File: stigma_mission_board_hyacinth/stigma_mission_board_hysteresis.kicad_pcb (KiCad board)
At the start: 4 copper layers, 50 x 150 mm, 209 parts, among them J1 DF40C-70DS-0.4V(51), J2 DF40HB(2.5)-10DS-0.4V(51), J7 SMA, J8 SMA, J9 JST-GH 4Pin, Q1 DMN2056U, Q2 DMN2056U, Q3 AOSP21321, Q4 DMN2056U, Q5 AOSP21321, Q6 DMN2056U, Q7 AOSP21321, Q8 DMN2056U, Q9 AOSP21321, U1 LAN8742A, U10 MCP2562-E-SN, U11 MCP2562-E-SN, U12 SN74HCS594, U13 INA181, U14 INA181, U15 INA181, U16 INA181, U2 INA181, U3 TPD4E1U06, U4 L7805, U5 L7805, U6 AZ1117H-ADJ, U7 AZ1117H-ADJ, U8 Ai-Thinker-Ra-01, U9 Ai-Thinker-Ra-01, Y1 25MHz

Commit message: Added more components to NEW pcb layout.
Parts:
- removed C37, C54: 1u, Capacitor_SMD:C_0603_1608Metric
- removed C38: 10u, Capacitor_SMD:C_0805_2012Metric
- removed C39, C41: 22u, Capacitor_SMD:C_0805_2012Metric
- removed C46, C48: 10u, Capacitor_SMD:C_1206_3216Metric
- removed C47, C49: 100n, Capacitor_SMD:C_0603_1608Metric
- removed C53: 4u7, Capacitor_SMD:C_0805_2012Metric
- removed D13: SS34, Diode_SMD:D_SMA
- removed D20, D23: NRVB130T1G, Diode_SMD:D_SOD-123
- removed D21, D24: LED, LED_SMD:LED_0603_1608Metric
- removed D22, D25: D, Diode_SMD:D_0603_1608Metric
- removed F5, F6, F7, F8: 10A, Fuse:Fuse_1206_3216Metric
- removed J11, J12, J3: ~, Connector_Molex:Molex_Micro-Fit_3.0_43045-0400_2x02_P3.00mm_Horizontal
- removed JP1: SolderJumper_2_Open, Jumper:SolderJumper-2_P1.3mm_Open_Pad1.0x1.5mm
- removed JP4, JP5: servo_switch, Stigma:SolderJumper-3_Open_RoundedPad2x2mm
- removed Q4, Q6: DMN2056U, Package_TO_SOT_SMD:SOT-23
- removed Q5, Q7: AOSP21321, Package_SO:SO-8_3.9x4.9mm_P1.27mm
- removed R49, R53: 10k, Resistor_SMD:R_0603_1608Metric
- removed R50, R52, R54, R56: 1k, Resistor_SMD:R_0603_1608Metric
- removed R51, R55: 60R, Resistor_SMD:R_0603_1608Metric
- removed Shunt2, Shunt3: 250mR 1%, Resistor_SMD:R_0805_2012Metric
- removed U14, U15: INA181, Package_TO_SOT_SMD:SOT-23-6
- C14, C15, C16, C17, C18, C19, C20, C21, D10, D11, D12, D5, D6, D7, D8, D9, R30, R31, R32, R33, R34, R35, R36, R37, U4, U5, U6, U7: moved to B.Cu
- J1, J2: moved to F.Cu
- moved R23 278.4 mm to (141.3, 192.2)
- moved R25 278.4 mm to (107.2, 192.7)
- moved R26 278.4 mm to (107.2, 189.6)
- moved R24 278.4 mm to (141.3, 189.2)
- moved C51 273.9 mm to (125.8, 243.7)
- moved C55 273.9 mm to (123.2, 242.4)
- moved D26 273.9 mm to (124.8, 236.5)
- moved D27 273.9 mm to (113.4, 228.6)
- moved F1 273.9 mm to (121.6, 243.4)
- moved JP6 273.9 mm to (120.8, 238.5)
- moved Q8 273.9 mm to (127.3, 231.1)
- moved Q9 273.9 mm to (120.4, 232.3)
- moved R58 273.9 mm to (124.9, 231.1)
- moved R60 273.9 mm to (116.8, 228.6)
- moved Shunt4 273.9 mm to (126.0, 238.6)
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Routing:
- net GND: track 58.5 -> 26.5 mm, vias 43 -> 22
- net Net-(U15-+): track 7.55 -> 0.00 mm
- net Net-(U14-+): track 6.38 -> 0.00 mm
- net Net-(D20-A): track 4.93 -> 0.00 mm
- net Net-(D23-A): track 4.75 -> 0.00 mm
- net /Recovery Output 4/recovery_switched: track 4.73 -> 0.00 mm
- net /Recovery Output2/recovery_switched: track 3.54 -> 0.00 mm
- net +3.3V: track 3.16 -> 0.00 mm
- net /Recovery Output2/high_current: track 2.54 -> 0.00 mm, vias 16 -> 0
- net /Recovery Output 4/high_current: track 2.54 -> 0.00 mm, vias 15 -> 0
- net /Recovery Output 4/servo_line: track 2.36 -> 0.00 mm
- net /Recovery Output2/servo_line: track 2.26 -> 0.00 mm
- net RECOVERY_4: track 1.86 -> 0.00 mm
- net RECOVERY_2: track 1.80 -> 0.00 mm
- net Net-(D24-A): track 1.39 -> 0.00 mm
- removed copper zone on B.Cu, net /Recovery Output 1/high_current
- removed copper zone on B.Cu, net /Recovery Output 4/high_current
- removed copper zone on F.Cu, net /Recovery Output 4/high_current
- removed copper zone on F.Cu, net /Recovery Output 4/recovery_switched
- removed copper zone on F.Cu, net /Recovery Output 4/servo_line
- removed copper zone on B.Cu, net /Recovery Output2/high_current
- removed copper zone on F.Cu, net /Recovery Output2/high_current
- removed copper zone on F.Cu, net /Recovery Output2/recovery_switched
- removed copper zone on F.Cu, net /Recovery Output2/servo_line
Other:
- board size 50 x 150 mm -> 16.4 x 9.5 mm
- board text removed: "LORA"
- board text removed: "recovery1"
- board text removed: "recovery2"
- board text removed: "recovery3"
- board text removed: "recovery4"
- board text removed: "take a look"
- board text removed: "todo: symmetrize"

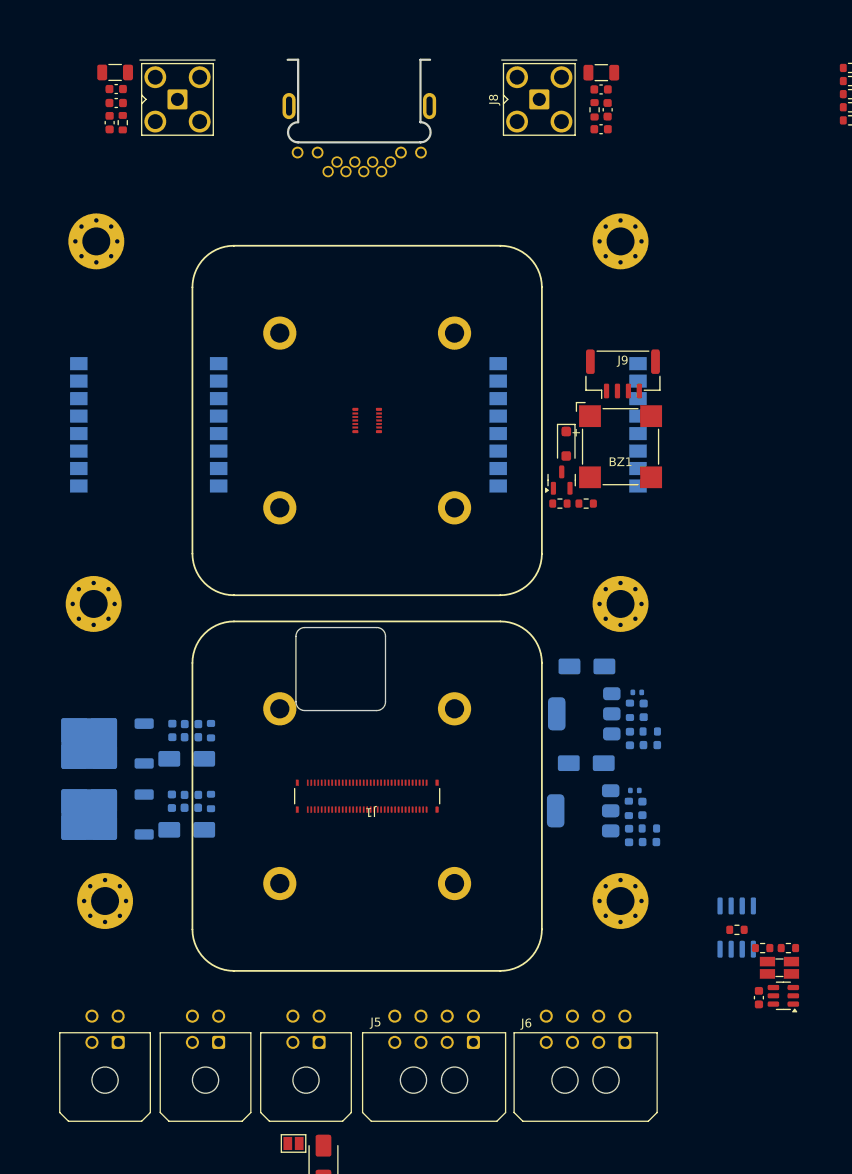
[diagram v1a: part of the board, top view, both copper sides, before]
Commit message: changed outer layout
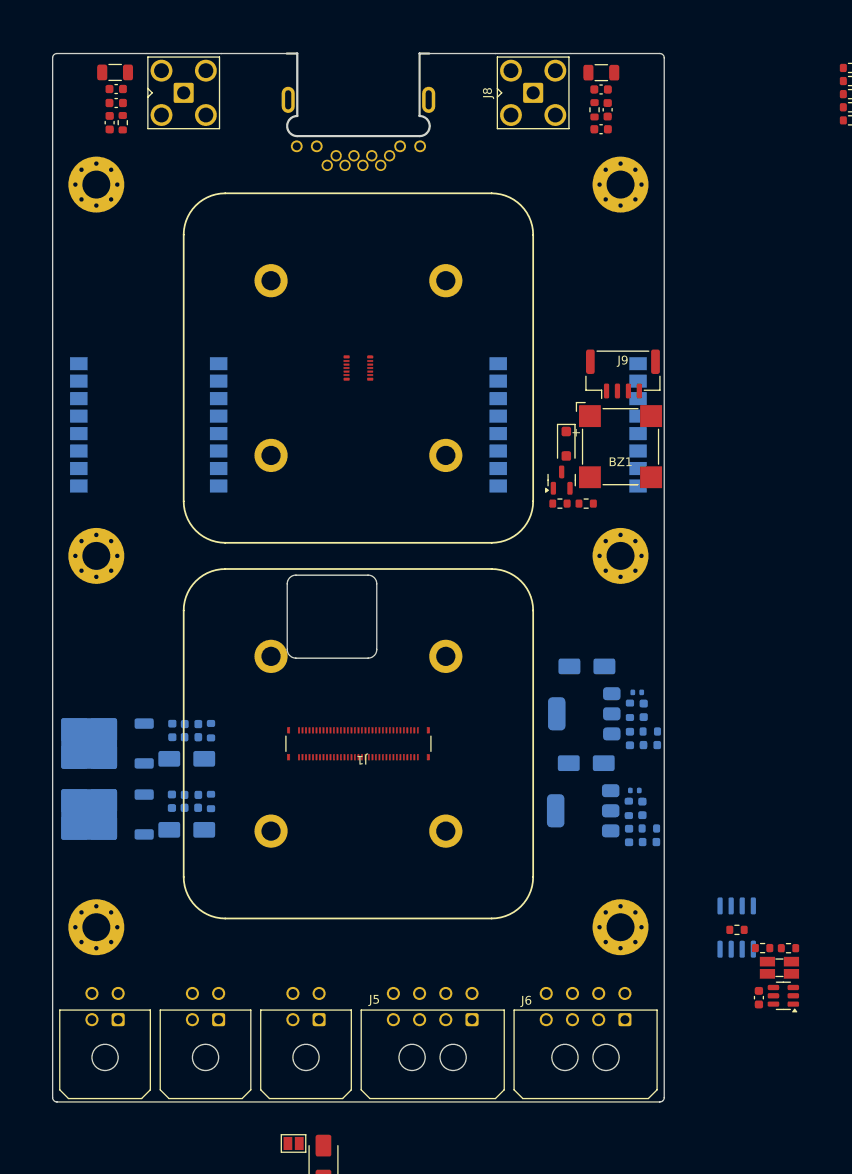
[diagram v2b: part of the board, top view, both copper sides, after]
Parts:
- moved H3 6.50 mm to (185.0, 142.0)
- moved H6 6.50 mm to (245.0, 142.0)
- moved J1 6.08 mm to (215.0, 206.0)
- moved J2 6.08 mm to (215.0, 163.0)
- moved H5 5.51 mm to (185.0, 184.5)
- moved H4 5.50 mm to (245.0, 184.5)
- moved H1 3.16 mm to (185.0, 227.0)
- moved H2 3.00 mm to (245.0, 227.0)
- moved J5 2.60 mm to (228.0, 237.6)
- moved J10 2.60 mm to (199.0, 237.6)
- moved J13 2.60 mm to (187.5, 237.6)
- moved J4 2.60 mm to (210.5, 237.6)
- moved J6 2.60 mm to (245.5, 237.6)
- moved J7 1.03 mm to (195.0, 131.5)
- moved J8 1.03 mm to (235.0, 131.5)
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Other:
- board size 16.4 x 9.5 mm -> 70 x 120 mm
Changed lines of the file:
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@@
 	(footprint "Resistor_SMD:R_0603_1608Metric"
 		(layer "F.Cu")
-		(at 264.2125 229.3875 180)
+		(at 264.225 229.4 180)
 		(descr "Resistor SMD 0603 (1608 Metric), square (rectangular) end terminal, IPC_7351 nominal, (Body size source: IPC-SM-782 page 72, https://www.pcb-3d.com/wordpress/wp-content/uploads/ipc-sm-782a_amendment_1_and_2.pdf), generated with kicad-footprint-generator")
 		(tags "resistor")
@@
 	)
 	(footprint "Connector_Molex:Molex_Micro-Fit_3.0_43045-0400_2x02_P3.00mm_Horizontal"
+		(locked yes)
 		(layer "F.Cu")
-		(at 210.5 240.18 180)
+		(at 210.5 237.58 180)
 		(descr "Molex Micro-Fit 3.0 Connector System, 43045-0400 (alternative finishes: 43045-040x), 2 Pins per row (https://www.molex.com/pdm_docs/sd/430450201_sd.pdf), generated with kicad-footprint-generator")
 		(tags "connector Molex Micro-Fit_3.0 horizontal")
@@
 	)
 	(footprint "MountingHole:MountingHole_3.2mm_M3_Pad_Via"
+		(locked yes)
 		(layer "F.Cu")
-		(at 186 224)
+		(at 185 227)
 		(descr "Mounting Hole 3.2mm, M3")
 		(tags "mounting hole 3.2mm m3")
@@
 	)
 	(footprint "Connector_Molex:Molex_Micro-Fit_3.0_43045-0800_2x04_P3.00mm_Horizontal"
+		(locked yes)
 		(layer "F.Cu")
-		(at 245.5 240.18 180)
+		(at 245.5 237.58 180)
 		(descr "Molex Micro-Fit 3.0 Connector System, 43045-0800 (alternative finishes: 43045-080x), 4 Pins per row (https://www.molex.com/pdm_docs/sd/430450201_sd.pdf), generated with kicad-footprint-generator")
 		(tags "connector Molex Micro-Fit_3.0 horizontal")
@@
 	)
 	(footprint "Connector_Coaxial:SMA_Amphenol_901-143_Horizontal"
+		(locked yes)
 		(layer "F.Cu")
-		(at 194.29 132.25)
+		(at 195 131.5)
 		(descr " Amphenol RF 901-143 https://www.amphenolrf.com/library/download/link/link_id/585682")
 		(tags "SMA THT Female Jack Horizontal")
@@
 			(remove_unused_layers yes)
 			(keep_end_layers yes)
-			(zone_layer_connections)
+			(zone_layer_connections "In1.Cu" "In2.Cu")
 			(net 3 "GND")
 			(pinfunction "Ext")
@@
 			(remove_unused_layers yes)
 			(keep_end_layers yes)
-			(zone_layer_connections)
+			(zone_layer_connections "In1.Cu" "In2.Cu")
 			(net 3 "GND")
 			(pinfunction "Ext")
@@
 			(remove_unused_layers yes)
 			(keep_end_layers yes)
-			(zone_layer_connections)
+			(zone_layer_connections "In1.Cu" "In2.Cu")
 			(net 3 "GND")
 			(pinfunction "Ext")
@@
 			(remove_unused_layers yes)
 			(keep_end_layers yes)
-			(zone_layer_connections)
+			(zone_layer_connections "In1.Cu" "In2.Cu")
 			(net 3 "GND")
 			(pinfunction "Ext")
@@
 	)
 	(footprint "MountingHole:MountingHole_3.2mm_M3_Pad_Via"
+		(locked yes)
 		(layer "F.Cu")
-		(at 245 190)
+		(at 245 184.5)
 		(descr "Mounting Hole 3.2mm, M3")
 		(tags "mounting hole 3.2mm m3")
@@
 	)
 	(footprint "Connector_Molex:Molex_Micro-Fit_3.0_43045-0400_2x02_P3.00mm_Horizontal"
+		(locked yes)
 		(layer "F.Cu")
-		(at 199 240.18 180)
+		(at 199 237.58 180)
 		(descr "Molex Micro-Fit 3.0 Connector System, 43045-0400 (alternative finishes: 43045-040x), 2 Pins per row (https://www.molex.com/pdm_docs/sd/430450201_sd.pdf), generated with kicad-footprint-generator")
 		(tags "connector Molex Micro-Fit_3.0 horizontal")
@@
 	)
 	(footprint "MountingHole:MountingHole_3.2mm_M3_Pad_Via"
+		(locked yes)
 		(layer "F.Cu")
-		(at 245 148.5)
+		(at 245 142)
 		(descr "Mounting Hole 3.2mm, M3")
 		(tags "mounting hole 3.2mm m3")
@@
 	)
 	(footprint "Connector_Coaxial:SMA_Amphenol_901-143_Horizontal"
+		(locked yes)
 		(layer "F.Cu")
-		(at 235.7 132.25)
+		(at 235 131.5)
 		(descr " Amphenol RF 901-143 https://www.amphenolrf.com/library/download/link/link_id/585682")
 		(tags "SMA THT Female Jack Horizontal")
@@
 			(remove_unused_layers yes)
 			(keep_end_layers yes)
-			(zone_layer_connections)
+			(zone_layer_connections "In1.Cu" "In2.Cu")
 			(net 3 "GND")
 			(pinfunction "Ext")
@@
 			(remove_unused_layers yes)
 			(keep_end_layers yes)
-			(zone_layer_connections)
+			(zone_layer_connections "In1.Cu" "In2.Cu")
 			(net 3 "GND")
 			(pinfunction "Ext")
@@
 			(remove_unused_layers yes)
 			(keep_end_layers yes)
-			(zone_layer_connections)
+			(zone_layer_connections "In1.Cu" "In2.Cu")
 			(net 3 "GND")
 			(pinfunction "Ext")
@@
 			(remove_unused_layers yes)
 			(keep_end_layers yes)
-			(zone_layer_connections)
+			(zone_layer_connections "In1.Cu" "In2.Cu")
 			(net 3 "GND")
 			(pinfunction "Ext")
@@
 	(footprint "Stigma:gps-board-only-inner-mounting-holes"
 		(layer "F.Cu")
-		(at 216 169 -90)
+		(at 215 163 -90)
 		(property "Reference" "J2"
 			(at 0.3 -2.5 270)
@@
 			(polygon
 				(pts
-					(xy 236.32 148.68) (xy 236.32 189.32) (xy 195.68 189.32) (xy 195.68 148.68)
+					(xy 235.32 142.68) (xy 235.32 183.32) (xy 194.68 183.32) (xy 194.68 142.68)
 				)
 			)
@@
 	)
 	(footprint "MountingHole:MountingHole_3.2mm_M3_Pad_Via"
+		(locked yes)
 		(layer "F.Cu")
-		(at 184.697056 190)
+		(at 185 184.5)
 		(descr "Mounting Hole 3.2mm, M3")
 		(tags "mounting hole 3.2mm m3")
@@
 	)
 	(footprint "Connector_Molex:Molex_Micro-Fit_3.0_43045-0800_2x04_P3.00mm_Horizontal"
+		(locked yes)
 		(layer "F.Cu")
-		(at 228.16 240.18 180)
+		(at 228 237.58 180)
 		(descr "Molex Micro-Fit 3.0 Connector System, 43045-0800 (alternative finishes: 43045-080x), 4 Pins per row (https://www.molex.com/pdm_docs/sd/430450201_sd.pdf), generated with kicad-footprint-generator")
 		(tags "connector Molex Micro-Fit_3.0 horizontal")
@@
 	)
 	(footprint "MountingHole:MountingHole_3.2mm_M3_Pad_Via"
+		(locked yes)
 		(layer "F.Cu")
-		(at 245 224)
+		(at 245 227)
 		(descr "Mounting Hole 3.2mm, M3")
 		(tags "mounting hole 3.2mm m3")
@@
 	)
 	(footprint "MountingHole:MountingHole_3.2mm_M3_Pad_Via"
+		(locked yes)
 		(layer "F.Cu")
-		(at 185 148.5)
+		(at 185 142)
 		(descr "Mounting Hole 3.2mm, M3")
 		(tags "mounting hole 3.2mm m3")
@@
 	)
 	(footprint "Connector_Molex:Molex_Micro-Fit_3.0_43045-0400_2x02_P3.00mm_Horizontal"
+		(locked yes)
 		(layer "F.Cu")
-		(at 187.5 240.18 180)
+		(at 187.5 237.58 180)
 		(descr "Molex Micro-Fit 3.0 Connector System, 43045-0400 (alternative finishes: 43045-040x), 2 Pins per row (https://www.molex.com/pdm_docs/sd/430450201_sd.pdf), generated with kicad-footprint-generator")
 		(tags "connector Molex Micro-Fit_3.0 horizontal")
@@
 	)
 	(footprint "Stigma:core-board-inner-mounting-holes"
+		(locked yes)
 		(layer "F.Cu")
-		(at 216 212 180)
+		(at 215 206 180)
 		(property "Reference" "J1"
 			(at -0.4 -1.85 180)
@@
 		(sheetname "/")
 		(sheetfile "stigma_mission_board_hysteresis.kicad_sch")
-		(attr smd exclude_from_bom)
+		(attr exclude_from_bom)
 		(fp_line
 			(start 20 15.25)
@@
 			(polygon
 				(pts
-					(xy 236.32 232.32) (xy 195.68 232.32) (xy 195.68 191.68) (xy 236.32 191.68)
+					(xy 235.32 226.32) (xy 194.68 226.32) (xy 194.68 185.68) (xy 235.32 185.68)
 				)
 			)
@@
 				(tracks not_allowed)
 				(vias not_allowed)
-				(pads not_allowed)
+				(pads allowed)
 				(copperpour not_allowed)
-				(footprints not_allowed)
+				(footprints allowed)
 			)
 			(placement
@@
 			(polygon
 				(pts
-					(xy 218.1 202.2) (xy 207.85 202.2) (xy 207.85 192.7) (xy 218.1 192.7)
+					(xy 217.1 196.2) (xy 206.85 196.2) (xy 206.85 186.7) (xy 217.1 186.7)
 				)
 			)
@@
 	)
 	(footprint "Stigma:RJ45-TH_MJ88B-B011-RVL11-P"
+		(locked yes)
 		(layer "B.Cu")
-		(at 215.1 136.7635)
+		(at 215 136.05)
 		(property "Reference" "RJ1"
 			(at 0 5.1 0)
@@
 		(layer "Cmts.User")
 	)
+	(gr_line
+		(start 206.8 127)
+		(end 199.3 127)
+		(stroke
+			(width 0.05)
+			(type default)
+		)
+		(locked yes)
+		(layer "Edge.Cuts")
+	)
+	(gr_arc
+		(start 249.5 127)
+		(mid 249.853553 127.146447)
+		(end 250 127.5)
+		(stroke
+			(width 0.05)
+			(type default)
+		)
+		(locked yes)
+		(layer "Edge.Cuts")
+	)
+	(gr_line
+		(start 249.5 247)
+		(end 180.5 247)
+		(stroke
+			(width 0.05)
+			(type default)
+		)
+		(locked yes)
+		(layer "Edge.Cuts")
+	)
+	(gr_line
+		(start 190.7 127)
+		(end 180.5 127)
+		(stroke
+			(width 0.05)
+			(type default)
+		)
+		(locked yes)
+		(layer "Edge.Cuts")
+	)
+	(gr_line
+		(start 239.3 127)
+		(end 249.5 127)
+		(stroke
+			(width 0.05)
+			(type default)
+		)
+		(locked yes)
+		(layer "Edge.Cuts")
+	)
+	(gr_arc
+		(start 180.5 247)
+		(mid 180.146447 246.853553)
+		(end 180 246.5)
+		(stroke
+			(width 0.05)
+			(type default)
+		)
+		(locked yes)
+		(layer "Edge.Cuts")
+	)
+	(gr_line
+		(start 180 127.5)
+		(end 180 246.5)
+		(stroke
+			(width 0.05)
+			(type default)
+		)
+		(locked yes)
+		(layer "Edge.Cuts")
+	)
+	(gr_line
+		(start 230.7 127)
+		(end 223.1 127)
+		(stroke
+			(width 0.05)
+			(type default)
+		)
+		(locked yes)
+		(layer "Edge.Cuts")
+	)
+	(gr_arc
+		(start 180 127.5)
+		(mid 180.146447 127.146447)
+		(end 180.5 127)
+		(stroke
+			(width 0.05)
+			(type default)
+		)
+		(locked yes)
+		(layer "Edge.Cuts")
+	)
+	(gr_line
+		(start 250 127.5)
+		(end 250 246.5)
+		(stroke
+			(width 0.05)
+			(type default)
+		)
+		(locked yes)
+		(layer "Edge.Cuts")
+	)
+	(gr_arc
+		(start 250 246.5)
+		(mid 249.853553 246.853553)
+		(end 249.5 247)
+		(stroke
+			(width 0.05)
+			(type default)
+		)
+		(locked yes)
+		(layer "Edge.Cuts")
+	)
 	(gr_text "shift"
 		(at 135.15 147.675 0)
@@
 		(min_thickness 0.25)
 		(filled_areas_thickness no)
-		(fill
+		(fill yes
 			(thermal_gap 0.5)
 			(thermal_bridge_width 0.5)
@@
 		(polygon
 			(pts
-				(xy 180 127.75) (xy 180 250) (xy 250 250) (xy 250 127.75)
+				(xy 180 127) (xy 180 247) (xy 250 247) (xy 250 127)
 			)
 		)
@@
 		(min_thickness 0.25)
 		(filled_areas_thickness no)
-		(fill
+		(fill yes
 			(thermal_gap 0.5)
 			(thermal_bridge_width 0.5)
@@
 		(polygon
 			(pts
-				(xy 250 127.75) (xy 180 127.75) (xy 180 250) (xy 250 250)
+				(xy 250 127) (xy 180 127) (xy 180 247) (xy 250 247)
 			)
 		)

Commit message: added 3d models and datasheets
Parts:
- RJ1: moved to F.Cu
- turned RJ1 to 180 degrees
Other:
- outline, holes or cut-outs redrawn
- board text added: "@TODO check if footprint is correct"
